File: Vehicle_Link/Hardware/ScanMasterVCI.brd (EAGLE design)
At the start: 53 x 39.4 mm, 91 parts, among them IC1 XMEGA32A4U, Q1 MMBT4403, Q10 ZXMP6A17G, Q11 MMBT3904, Q12 MMBT3904, Q13 MMBT3904, Q2 MMBT3904, Q3 MMBT3904, Q4 MMBT3904, Q5 MMBT3904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

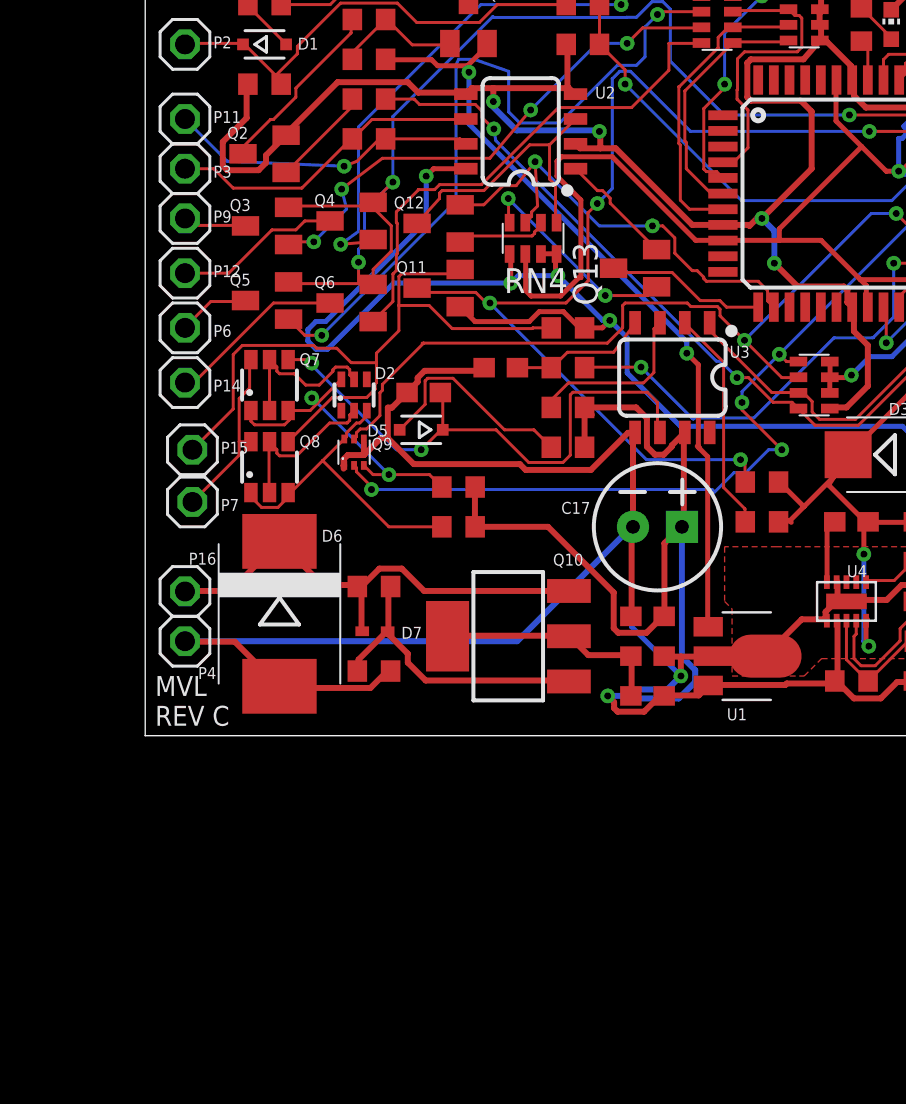
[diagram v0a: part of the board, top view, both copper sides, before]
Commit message: Deleted MOSFETs. They don't appear to work well with ISO9141. I need another way to switch between 5V/12V. Probably going to switch to simple transistors.
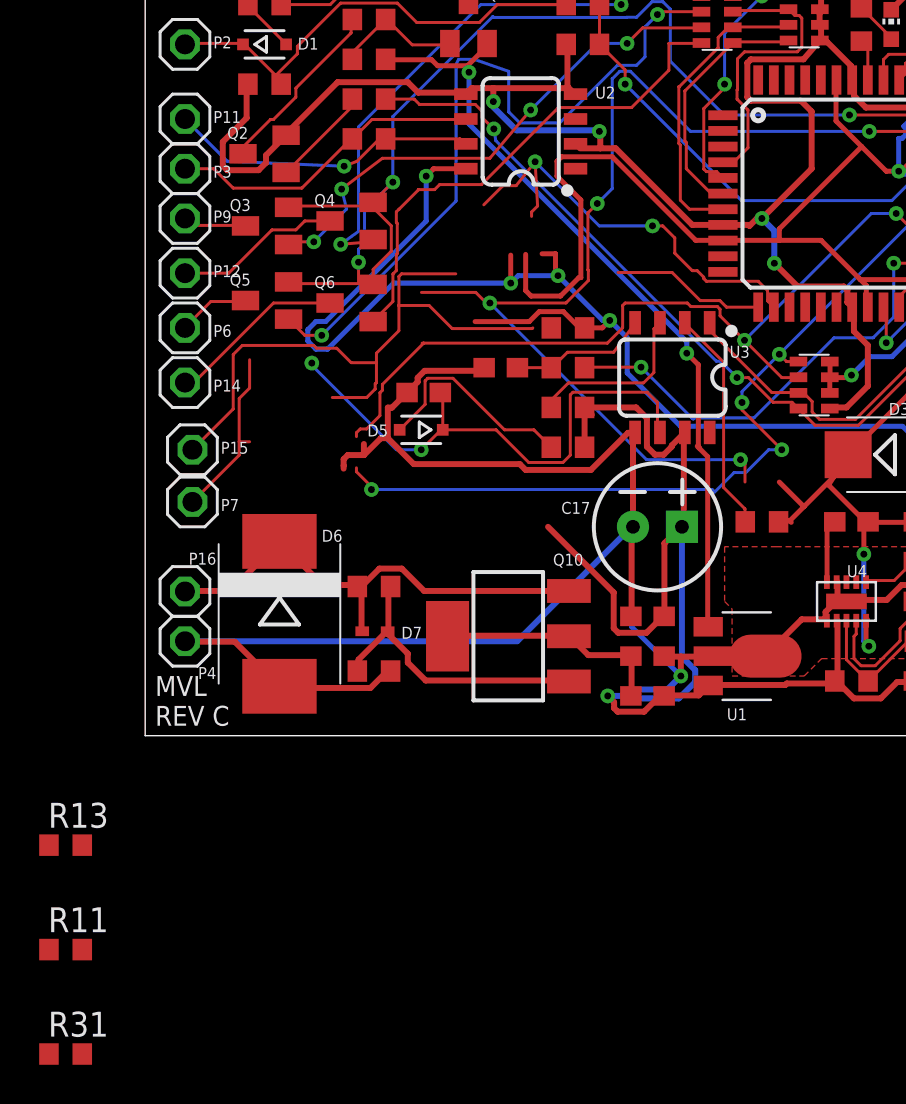
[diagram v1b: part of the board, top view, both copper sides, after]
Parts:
- removed D2: BZX84C2V4S, customics:SOT363
- removed Q11, Q12, Q13: MMBT3904, semicon-smd-ipc:SOT23
- removed Q7, Q8: NDC7002N, customics:SSOT6
- removed Q9: NTZD5110N, customics:SOT563
- removed R12, R9: 9.09M, adafruit:R0603
- removed RN4: 1k, resistor-net:CTS742C083
- added R13: 1k, adafruit:R0603
- added R31: 2k, adafruit:R0603
- moved R11 42.8 mm to (-4.06, -10.9)
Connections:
- removed net N$1: D2.2, Q8.2, Q8.5
- removed net N$11: D2.6, Q7.1, Q7.3, Q9.3, R9.1
- removed net N$32: Q12.3, RN4.1, U2.3
- removed net N$33: Q12.1, RN4.2
- removed net N$34: Q13.2, U2.1
- removed net N$35: Q13.1, RN4.4
- removed net N$4: D2.5, Q7.2, Q7.5
- removed net N$5: D2.3, Q8.1, Q8.3, Q9.6, R12.1
- net +12V: no longer R12.2, R9.2
- net +3V3: now also R13.2; no longer R11.2, RN4.6
- net +5V: now also U2.2; no longer Q11.1, RN4.5, RN4.7, RN4.8
- net CCD-RX: no longer Q13.3
- net CCD-TX: now also R13.1, U2.3; no longer Q12.2, RN4.3
- net GND: now also R31.2; no longer Q9.1, Q9.4, U2.2
- net ISO-K: no longer Q7.4
- net ISO-K-EN: no longer Q9.5
- net J1962-15: now also R11.1; no longer Q11.2, Q8.4
- net J1962-7: no longer Q7.6, Q8.6
- net SCI-A-TX-EN: no longer Q9.2
- net SCI-RX: now also R11.2, R31.1; no longer Q11.3, R11.1
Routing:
- net N$11: track 17.0 -> 0.00 mm, vias 2 -> 0
- net N$5: track 16.6 -> 0.00 mm
- net N$32: track 14.6 -> 0.00 mm
- net N$35: track 11.2 -> 0.00 mm, vias 2 -> 0
- net N$4: track 8.55 -> 0.00 mm
- net N$1: track 8.51 -> 0.00 mm
- net N$34: track 6.00 -> 0.00 mm
- net +12V: track 82.0 -> 76.3 mm
- net N$33: track 4.79 -> 0.00 mm
- net J1962-15: track 37.0 -> 32.5 mm
- net CCD-TX: track 24.9 -> 23.2 mm
- net +5V: track 99.7 -> 98.5 mm
- net ISO-K: track 29.2 -> 28.1 mm
- net GND: track 292.1 -> 291.4 mm

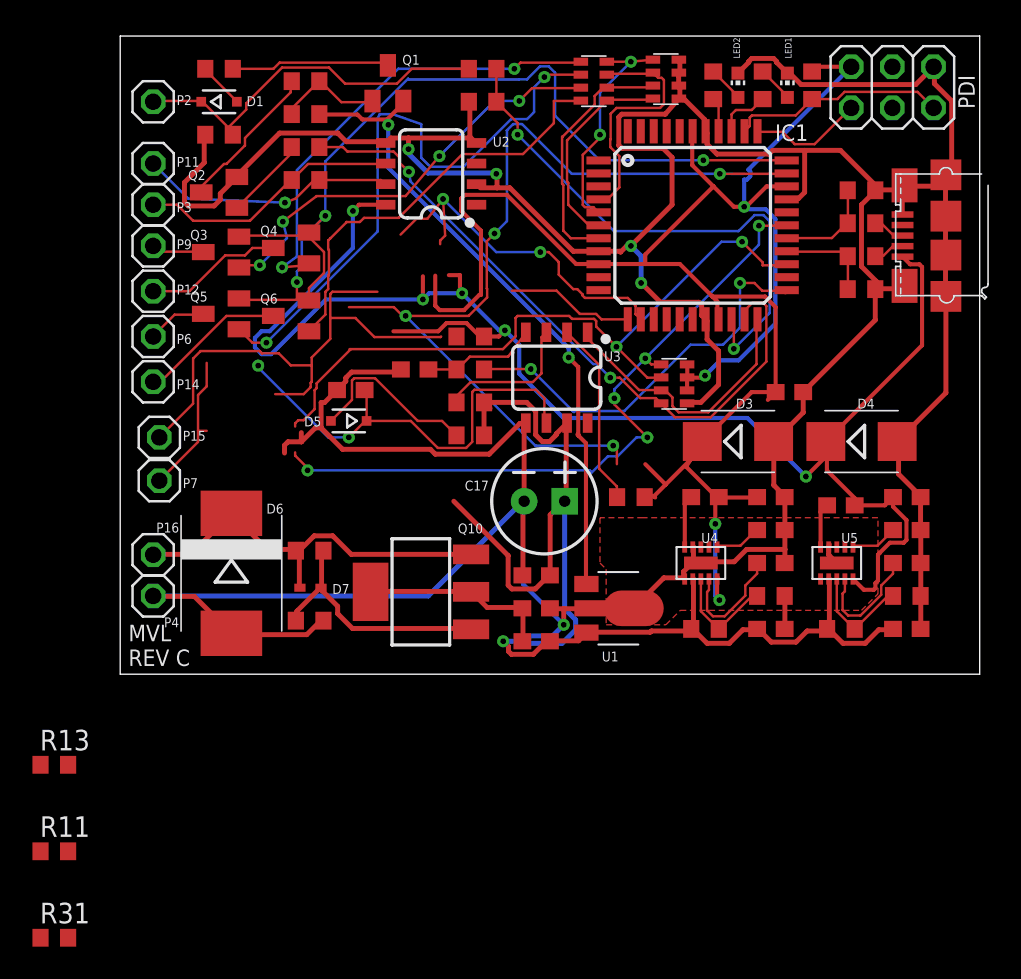
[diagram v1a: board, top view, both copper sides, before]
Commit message: Re-ran a few more data traces for style. Laid out everything on the board with latest schematic.
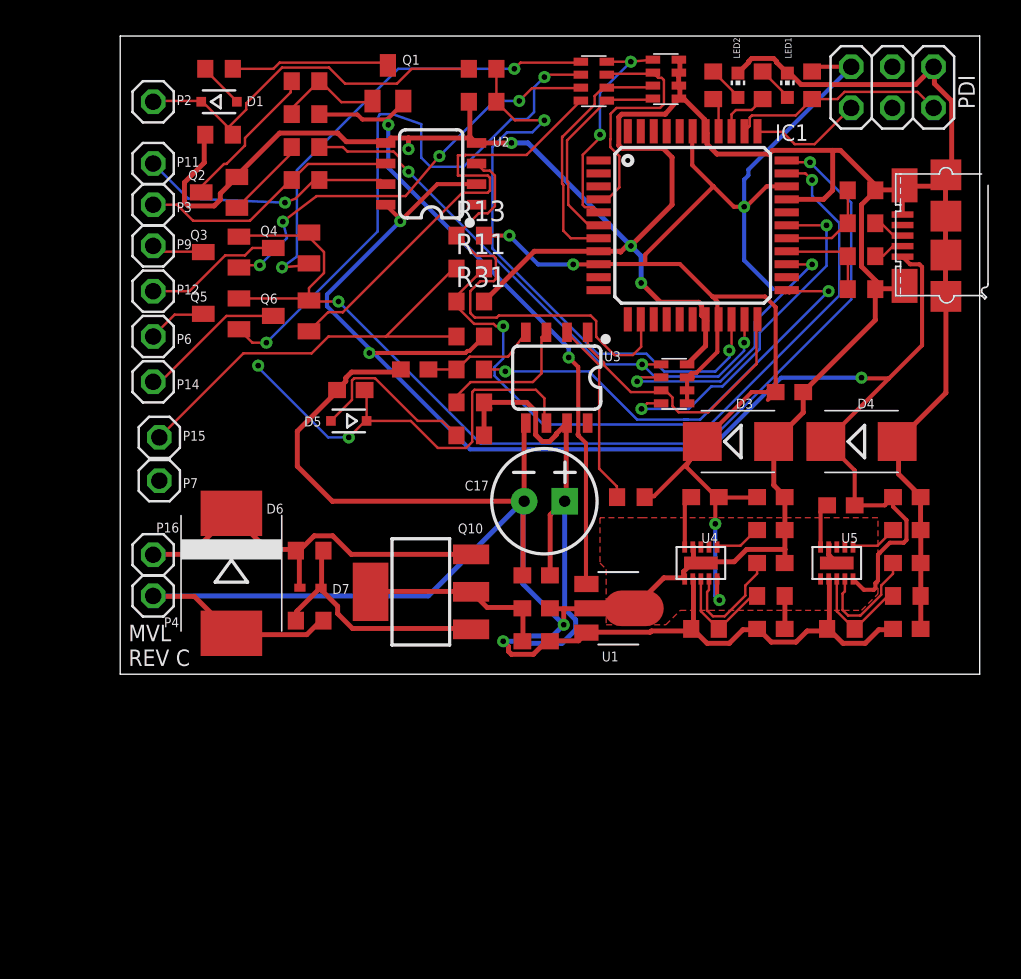
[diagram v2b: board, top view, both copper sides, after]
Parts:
- moved R31 46.9 mm to (21.6, 23.0)
- moved R11 44.2 mm to (21.6, 25.0)
- moved R13 41.5 mm to (21.6, 27.1)
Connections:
- net +3V3: now also RN3.5; no longer RN3.8
- net GND: now also RN3.8; no longer RN3.5
- net J1850VPW-TX: now also RN3.1; no longer RN3.4
- net SCI-A-TX-EN: now also RN3.4; no longer RN3.1
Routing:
- net ISO-K-EN: track 42.8 -> 17.9 mm
- net SCI-A-TX-EN: track 43.8 -> 22.0 mm, vias 5 -> 2
- net +3V3: track 116.8 -> 96.2 mm, vias 4 -> 5
- net SCI-RX: track 57.6 -> 45.0 mm, vias 4 -> 2
- net +12V: track 76.3 -> 66.7 mm
- net J1962-7: track 9.01 -> 0.00 mm
- net CCD-RX: track 7.99 -> 0.09 mm
- net SCI-TX: track 59.3 -> 65.5 mm, vias 3 -> 2
- net J1850VPW-TX: track 42.0 -> 36.0 mm, vias 2 -> 3
- net +5V: track 98.5 -> 92.9 mm, vias 5 -> 3
- net J1962-15: track 32.5 -> 27.0 mm
- net CCD-TX: track 23.2 -> 28.2 mm, vias 2 -> 0
- net ISO-K-TX: track 25.4 -> 29.4 mm
- net GND: track 291.4 -> 294.2 mm
- net J1850VPW-RX: track 33.8 -> 36.1 mm
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
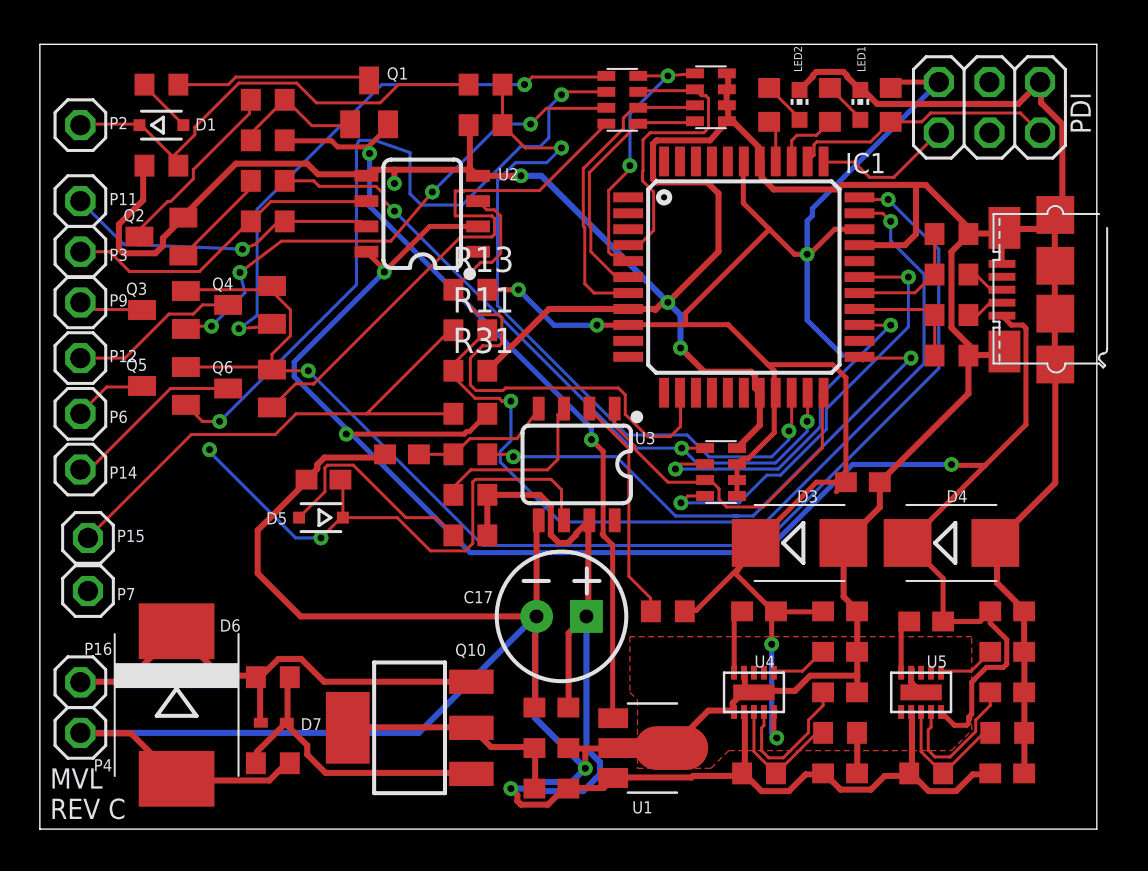
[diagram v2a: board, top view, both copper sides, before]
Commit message: Based on testing I did previously, added new circuits to hopefully finish out the CCD, SCI, and ISO9141. J1850 still needs work.
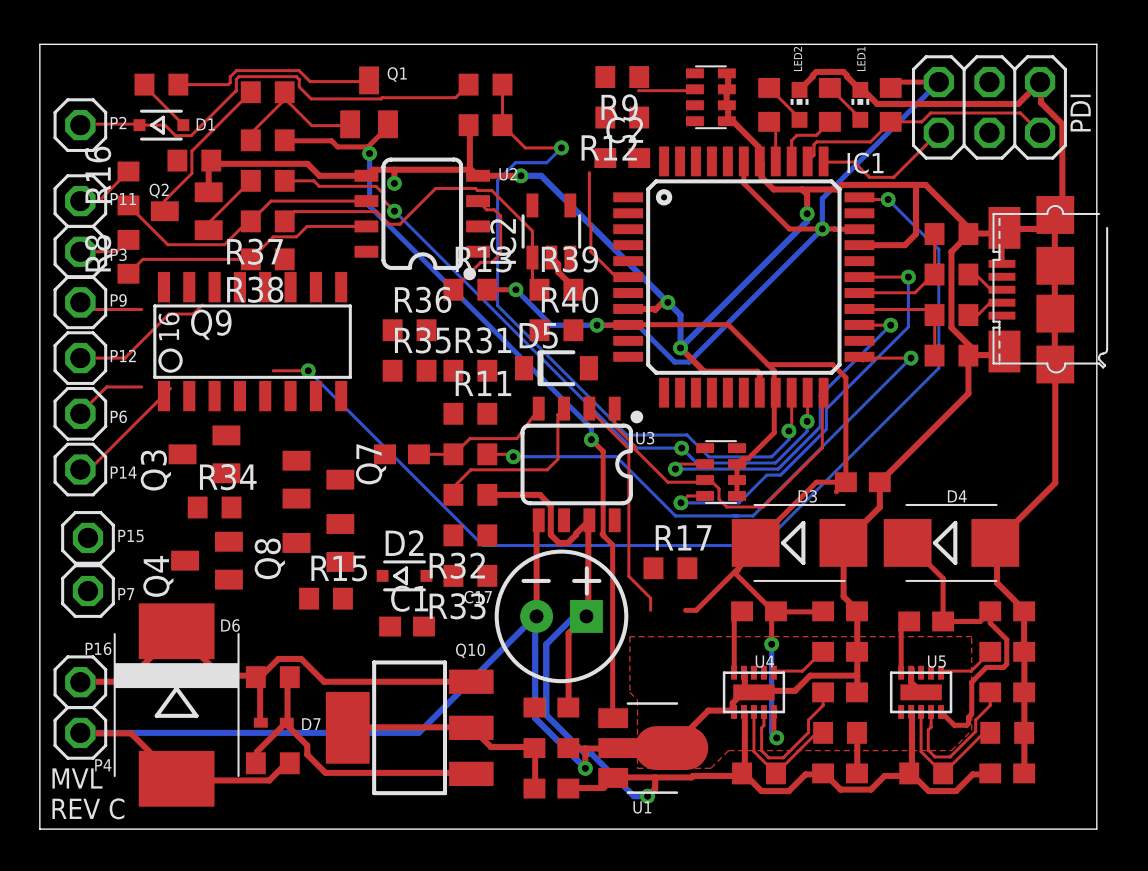
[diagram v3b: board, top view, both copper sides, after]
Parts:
- removed C5: 220pF, adafruit:C0603
- removed Q5, Q6: MMBT3904, semicon-smd-ipc:SOT23
- removed RN1: 1k, resistor-net:CTS742C083
- added C1, C2: 220pF, adafruit:C0603
- added D2: 1N4148WX, diode:SOD323-R
- added IC2: TL331, linear:DBV-R-PDSO-G5
- added Q7: MMBT3904, semicon-smd-ipc:SOT23
- added Q8: MMBT4403, transistor-pnp:SOT23-BEC
- added Q9: MMPQ3904, customics:SO-16
- added R12, R32, R33, R34, R35, R36, R9: 1k, adafruit:R0603
- added R37: 27.4k, adafruit:R0603
- added R38: 40.2k, adafruit:R0603
- added R39, R40: 1M, adafruit:R0603
- D5: value 1N4148WX -> 1N4148W-7-F; device diode:SOD323-R -> customics:SOD123FL
- Q4: value MMBT3904 -> MMBT4403; device semicon-smd-ipc:SOT23 -> transistor-pnp:SOT23-BEC
- R16: value 1k -> 100
- R8: value 120 -> 100
- moved R16 20.5 mm to (4.45, 32.1), turned to 90 degrees
- moved R15 17.2 mm to (14.4, 11.6), turned to 0 degrees
- moved D5 14.0 mm to (25.9, 23.1), turned to 0 degrees
- moved Q4 13.0 mm to (8.38, 13.5)
- moved R17 10.2 mm to (31.6, 13.1), turned to 0 degrees
- moved Q3 7.52 mm to (8.26, 18.8)
- moved R8 7.21 mm to (4.45, 28.7), turned to 90 degrees
- moved R11 4.19 mm to (21.6, 20.8)
- moved Q2 1.80 mm to (7.37, 31.0)
- moved R5 1.67 mm to (7.75, 33.5), turned to 180 degrees
- moved R4 0.38 mm to (11.4, 37.0)
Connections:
- removed net ISO-K: C5.1, D5.C, U3.6
- removed net SCI-RX: IC1.32, R11.2, R31.1
- removed net SCI-TX: IC1.33, Q3.2, Q4.2, Q5.2, Q6.2
- new net N$1: Q9.13, Q9.15, R9.2
- new net N$11: D2.A, R33.2
- new net N$32: R16.1, R37.2, U2.6
- new net N$33: R38.2, R8.1, U2.7
- new net N$34: IC2.1, R37.1, R39.1
- new net N$35: IC2.3, R38.1, R40.1
- new net N$36: D5.A, R40.2
- new net N$4: Q7.3, R15.1, R32.2
- new net N$5: Q9.11, Q9.9, R12.2
- new net SCI-A-EN: R9.1, RN2.1
- new net SCI-A-RX-EN: IC1.14, Q3.1
- new net SCI-B-EN: R12.1, RN2.2
- new net SCI-B-RX-EN: IC1.15
- new net SCI-ENGINE-RX: IC1.32
- new net SCI-ENGINE-TX: IC1.33, Q9.12, Q9.16
- new net SCI-TRANS-RX: IC1.16, R11.2, R31.1
- new net SCI-TRANS-TX: IC1.17, Q9.10, Q9.14
- net +12V: now also R32.1, R33.1; no longer R17.1
- net +3V3: now also C2.1, IC2.5, RN3.8; no longer R15.1
- net +5V: now also R35.2, R36.2; no longer R16.2
- net CCD-RX: now also D5.C, IC2.4, RN3.1
- net GND: now also C1.2, C2.2, IC2.2, Q3.2, Q7.2, R39.2; no longer C5.2, RN3.8
- net ISO-K-EN: now also R17.2, U3.2
- net J1850VPW-TX: now also RN2.3; no longer RN3.1
- net J1962-11: now also R16.2; no longer R8.2, U2.7
- net J1962-12: now also Q9.5, Q9.6; no longer Q4.3
- net J1962-14: now also Q9.3, Q9.4; no longer Q6.3
- net J1962-15: no longer R16.1
- net J1962-3: now also R8.2; no longer R8.1, U2.6
- net J1962-6: now also Q9.1, Q9.2; no longer Q5.3
- net J1962-7: now also Q4.C, Q8.C, U3.6
- net J1962-9: now also Q9.7, Q9.8; no longer Q3.3
- net N$13: now also Q7.1, R17.1; no longer Q4.1, RN1.1
- net N$21: now also C1.1, D2.C, Q8.E; no longer Q5.1, RN1.2
- net N$22: now also Q4.B, R34.2; no longer Q3.1, RN1.3
- net N$23: now also Q3.3, R34.1, R35.1; no longer Q6.1, RN1.4
- net N$31: now also Q4.E, R36.1; no longer D5.A, R17.2
- net N$8: now also Q8.B; no longer U3.2
- net SCI-A-ENGINE-EN: no longer RN1.7, RN2.2
- net SCI-A-TRANS-EN: no longer RN1.5, RN2.4
- net SCI-B-ENGINE-EN: no longer RN1.8, RN2.1
- net SCI-B-TRANS-EN: no longer RN1.6, RN2.3
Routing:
- net +5V: track 92.9 -> 16.2 mm, vias 3 -> 0
- net SCI-TX: track 65.5 -> 0.00 mm, vias 2 -> 0
- net GND: track 294.2 -> 237.3 mm, vias 5 -> 6
- net SCI-ENGINE-TX: track 0.00 -> 51.7 mm, vias 0 -> 2
- net SCI-RX: track 45.0 -> 0.00 mm, vias 2 -> 0
- net N$21: track 37.1 -> 0.00 mm, vias 2 -> 0
- net N$13: track 28.5 -> 0.00 mm, vias 2 -> 0
- net ISO-K: track 28.1 -> 0.00 mm, vias 2 -> 0
- net N$23: track 27.9 -> 0.00 mm
- net J1962-15: track 27.0 -> 0.00 mm
- net N$22: track 26.6 -> 0.00 mm, vias 4 -> 0
- net CCD-TX: track 28.2 -> 6.45 mm
- net N$34: track 0.00 -> 17.8 mm
- net SCI-A-ENGINE-EN: track 15.6 -> 0.00 mm
- net SCI-B-TRANS-EN: track 16.0 -> 0.55 mm
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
